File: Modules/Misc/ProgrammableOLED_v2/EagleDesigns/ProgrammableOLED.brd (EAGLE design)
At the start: 100 x 80 mm, 17 parts, among them U2 ATMEGA328P_TQFP

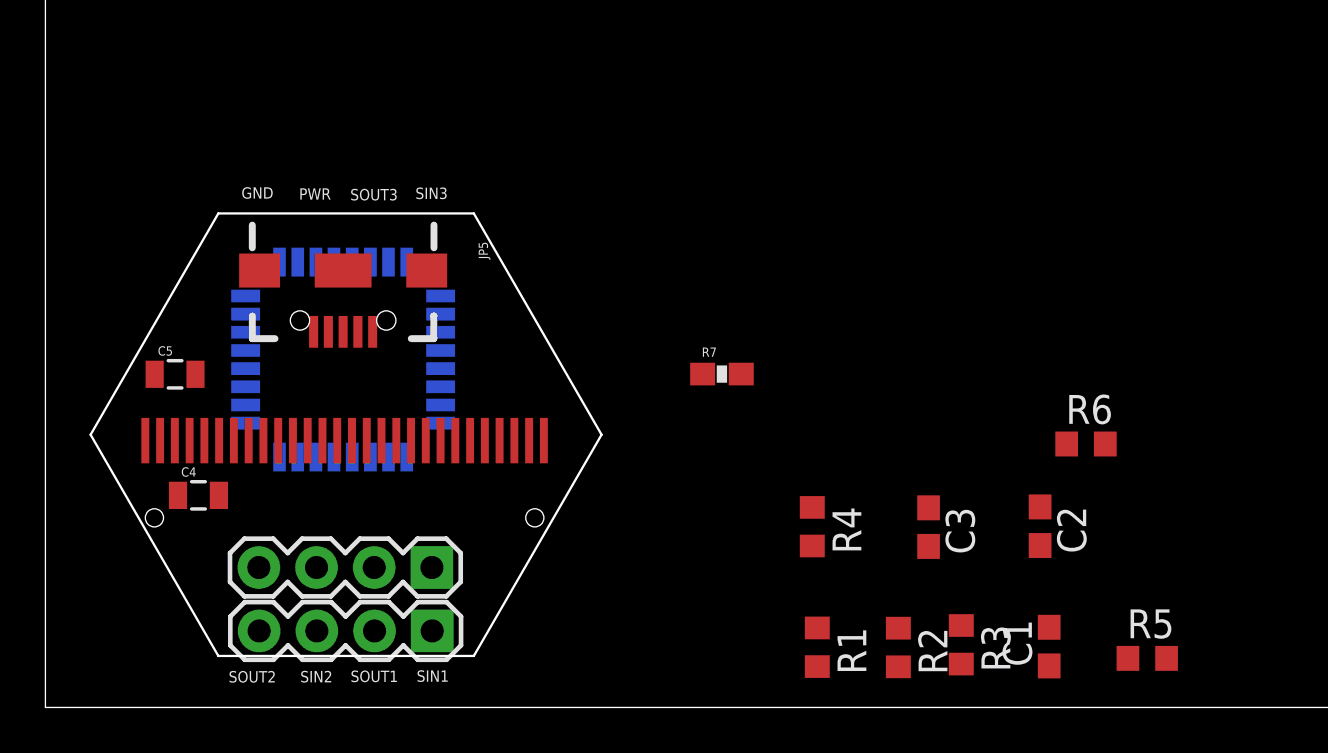
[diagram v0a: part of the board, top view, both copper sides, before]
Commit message: updated the top PCB of the programmable module with a bigger PCB
TODO: iterate and refine the top PCB
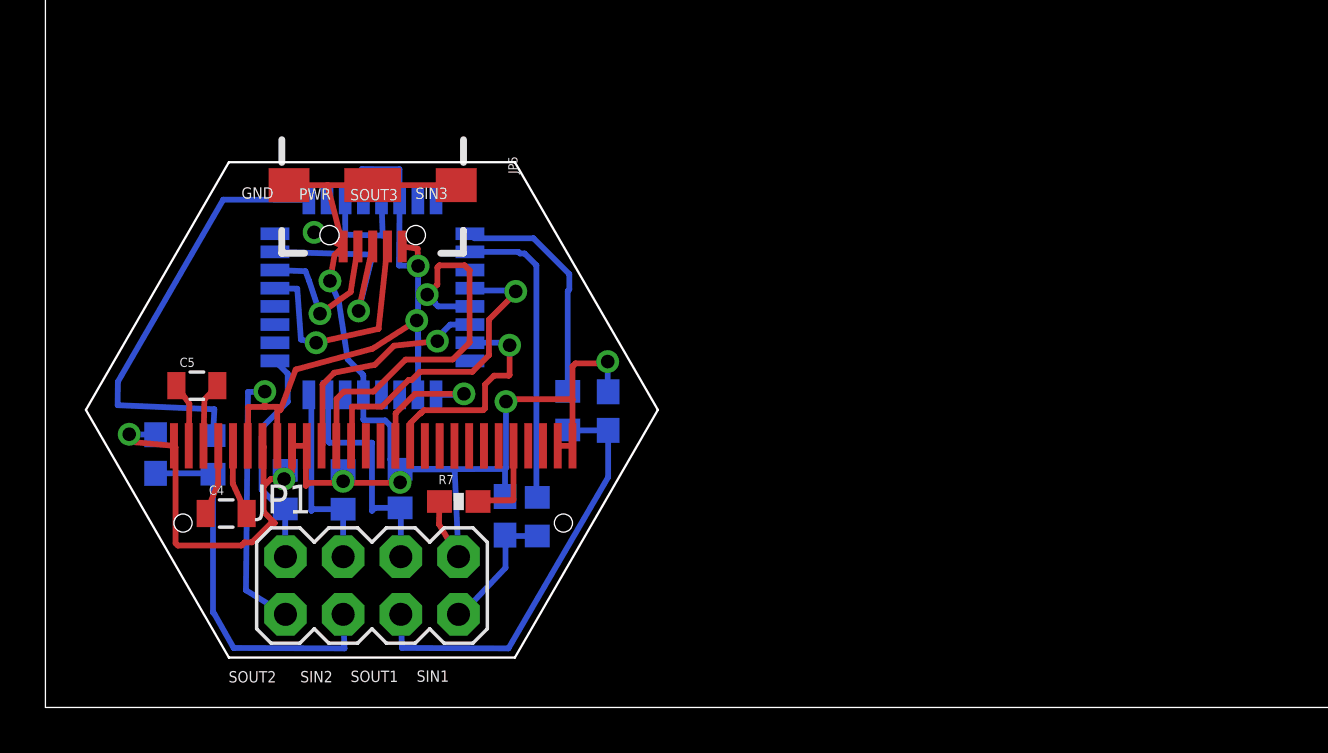
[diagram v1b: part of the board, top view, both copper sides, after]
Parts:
- removed JP2: (no value), SparkFun-Connectors:1X04
- JP1: device SparkFun-Connectors:1X04 -> SparkFun-Connectors:2X4
- moved C3 34.2 mm to (4.85, 11.2), flipped to the bottom, turned to 90 degrees
- moved R5 27.8 mm to (23.0, 13.1), flipped to the bottom, turned to 90 degrees
- moved R4 26.6 mm to (7.38, 11.1), flipped to the bottom, turned to 90 degrees
- moved R3 25.6 mm to (15.6, 9.64), flipped to the bottom
- moved R2 25.4 mm to (13.1, 9.58), flipped to the bottom
- moved R1 24.4 mm to (10.6, 9.59), flipped to the bottom
- moved R6 24.4 mm to (21.7, 8.40), flipped to the bottom, turned to 90 degrees
- moved C2 23.6 mm to (20.2, 8.44), flipped to the bottom, turned to 90 degrees
- moved C1 22.0 mm to (24.8, 13.1), flipped to the bottom
- moved R7 12.9 mm to (18.2, 9.07)
- moved JP5 3.98 mm to (14.4, 23.0)
- moved JP1 3.32 mm to (14.4, 5.37), turned to 0 degrees
- moved U2 3.03 mm to (14.4, 18.1), turned to 270 degrees
- moved C4 1.46 mm to (7.96, 8.54)
- moved OLED1 1.28 mm to (5.66, 11.5)
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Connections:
- net GND: now also JP1.8; no longer JP2.1
- net SIN1: now also JP1.6; no longer JP2.2
- net SIN2: now also JP1.4; no longer JP2.3
- net SIN3: now also JP1.2; no longer JP2.4
- net SOUT2: now also JP1.5; no longer JP1.2
- net SOUT3: now also JP1.7; no longer JP1.1
- net VCC: now also JP1.1; no longer JP1.4
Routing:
- net GND: track 0.00 -> 84.3 mm, vias 0 -> 8
- net VCC: track 0.00 -> 41.8 mm, vias 0 -> 3
- net OUT1: track 0.00 -> 19.5 mm
- net SOUT2: track 0.00 -> 18.7 mm
- net OLED-RST: track 0.00 -> 17.2 mm, vias 0 -> 1
- net SOUT1: track 0.00 -> 16.8 mm
- net OLED-D/C: track 0.00 -> 14.1 mm, vias 0 -> 1
- net OUT3: track 0.00 -> 13.4 mm
- net OLED-CS: track 0.00 -> 10.5 mm, vias 0 -> 1
- net SIN1: track 0.00 -> 10.5 mm
- net RESET: track 0.00 -> 10.4 mm, vias 0 -> 1
- net OUT2: track 0.00 -> 10.3 mm
- net OLED-MOSI: track 0.00 -> 9.97 mm, vias 0 -> 1
- net SIN3: track 0.00 -> 9.88 mm
- net TX: track 0.00 -> 9.77 mm, vias 0 -> 1
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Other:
- outline, holes or cut-outs redrawn

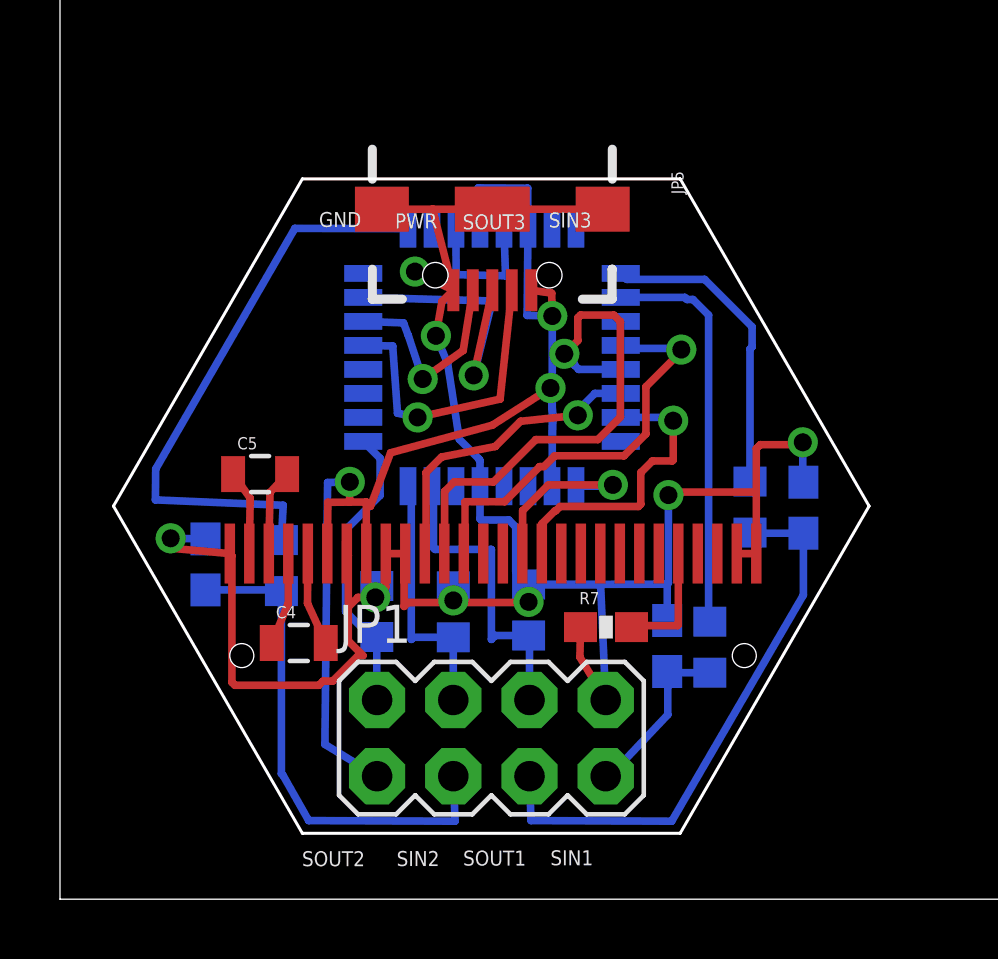
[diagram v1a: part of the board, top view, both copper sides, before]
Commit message: updated the Programmable OLED PCB. now cleaner, need to go a final iteration on it
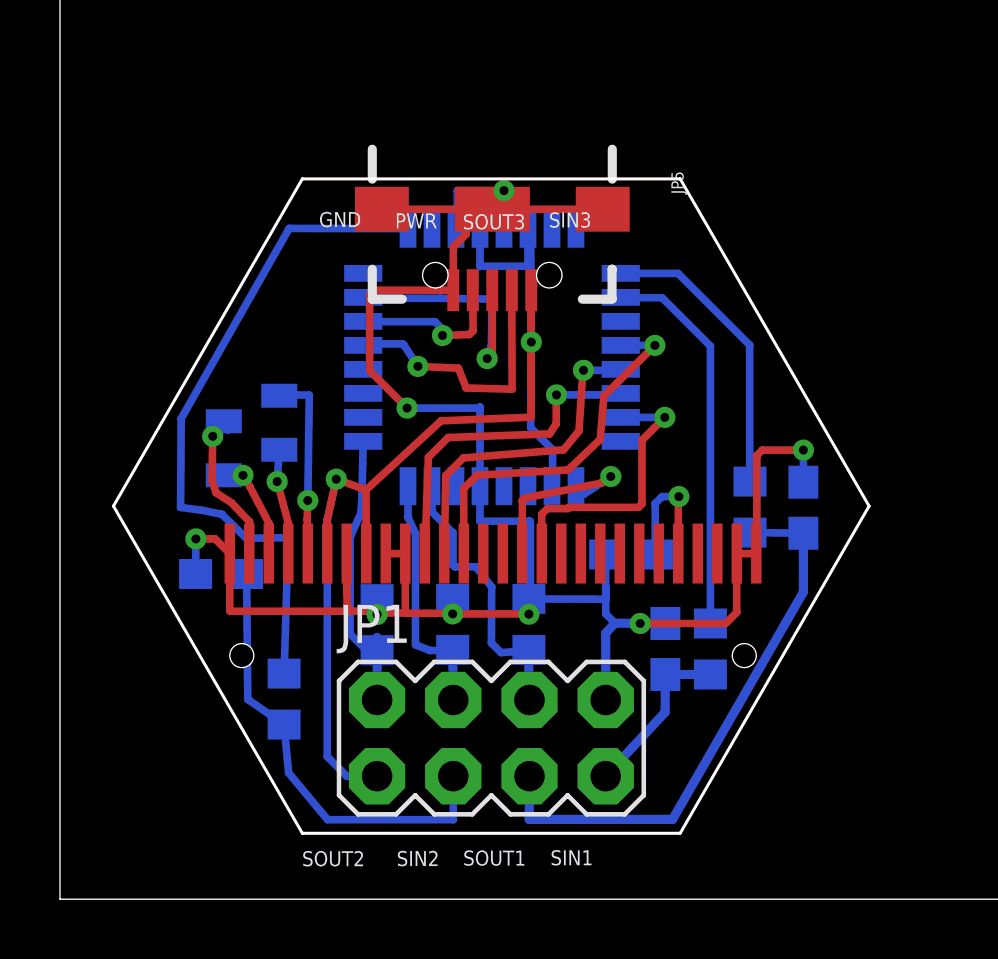
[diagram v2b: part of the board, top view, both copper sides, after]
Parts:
- moved C4 7.37 mm to (7.31, 15.9), flipped to the bottom, turned to 90 degrees
- moved R4 4.45 mm to (7.47, 6.67)
- moved R7 2.56 mm to (19.0, 11.5), flipped to the bottom, turned to 180 degrees
- moved C5 1.48 mm to (5.46, 15.0), flipped to the bottom, turned to 270 degrees
- moved C3 0.61 mm to (5.37, 10.8), turned to 0 degrees
- moved R3 0.48 mm to (15.6, 9.16)
- moved R1 0.44 mm to (10.6, 9.15)
- moved R2 0.42 mm to (13.1, 9.16)
- moved C2 0.12 mm to (20.2, 8.34)
- moved R6 0.06 mm to (21.7, 8.34)
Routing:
- net GND: track 84.3 -> 76.8 mm
- net OLED-RST: track 17.2 -> 10.9 mm
- net C1N: track 3.11 -> 6.30 mm, vias 0 -> 1
- net OUT1: track 19.5 -> 22.6 mm
- net C2P: track 2.83 -> 5.90 mm, vias 0 -> 1
- net SOUT1: track 16.8 -> 14.9 mm
- net OLED-D/C: track 14.1 -> 12.3 mm
- net RX: track 7.01 -> 5.38 mm
- net RESET: track 10.4 -> 9.13 mm
- net VCC: track 41.8 -> 40.6 mm, vias 3 -> 2
- net SIN1: track 10.5 -> 9.51 mm
- net TX: track 9.77 -> 8.84 mm
- net C2N: track 2.88 -> 3.53 mm, vias 0 -> 1
- net IREF: track 3.96 -> 4.51 mm, vias 0 -> 1
- net OLED-CS: track 10.5 -> 11.1 mm
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
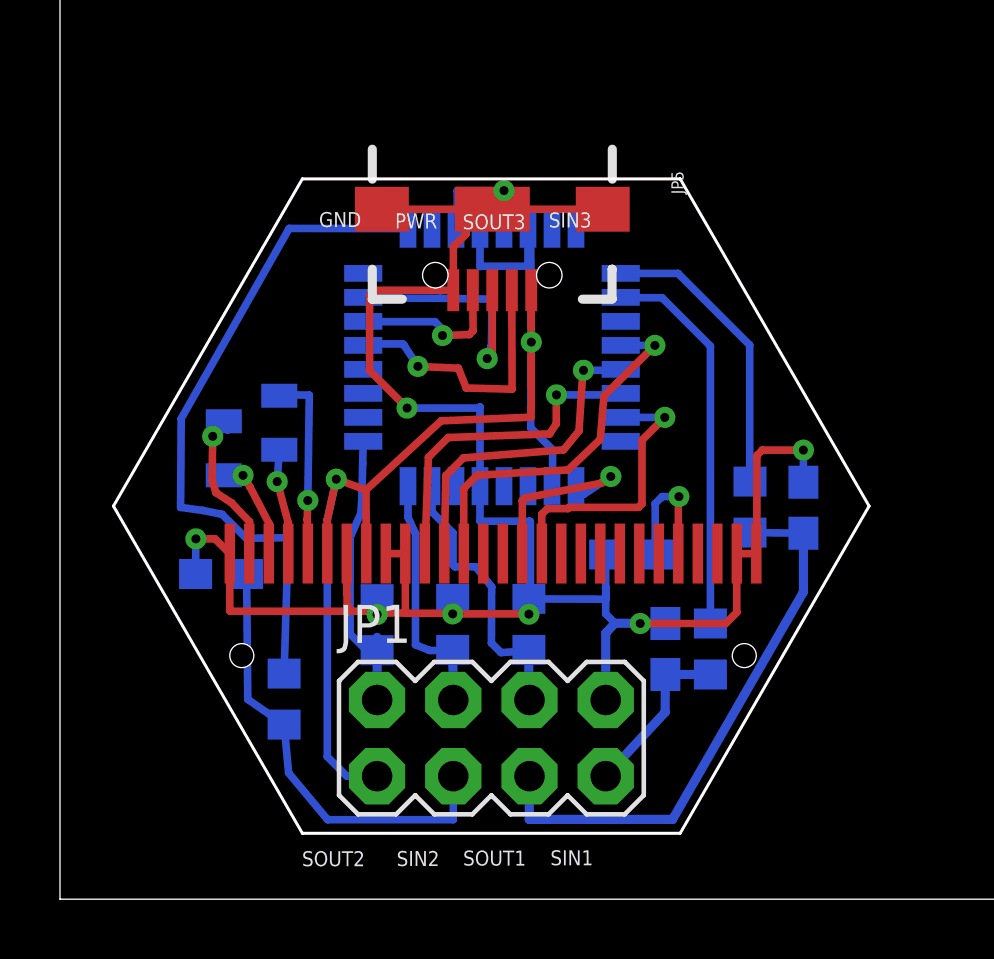
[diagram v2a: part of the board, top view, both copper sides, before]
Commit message: updated the PCB
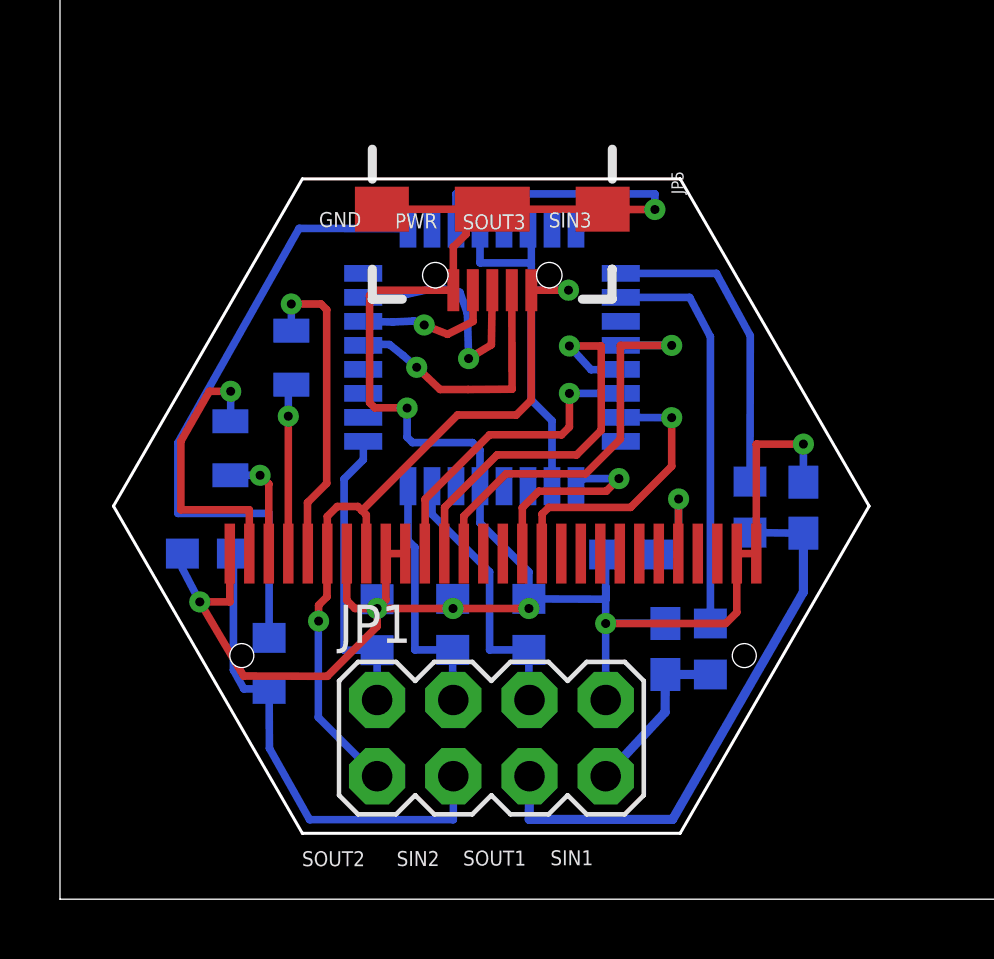
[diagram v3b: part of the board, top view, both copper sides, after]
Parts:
- moved C4 2.21 mm to (7.71, 18.1)
- moved R4 1.29 mm to (6.97, 7.86)
- moved C3 0.81 mm to (4.93, 11.5)
- moved C5 0.22 mm to (5.68, 15.0)
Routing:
- net GND: track 76.8 -> 86.2 mm
- net C1N: track 6.30 -> 10.5 mm
- net C2P: track 5.90 -> 9.66 mm
- net VCC: track 40.6 -> 37.7 mm
- net OLED-RST: track 10.9 -> 13.8 mm
- net C1P: track 3.51 -> 5.67 mm
- net OLED-D/C: track 12.3 -> 14.1 mm
- net SOUT1: track 14.9 -> 16.4 mm
- net OUT1: track 22.6 -> 21.4 mm
- net OLED-CS: track 11.1 -> 10.5 mm
- net TX: track 8.84 -> 8.24 mm
- net OUT2: track 9.84 -> 10.4 mm
